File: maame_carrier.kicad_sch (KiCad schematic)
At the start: 18 parts, among them J1 To Kakute H7 V1.5: full left 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, J10 FS-iA10B iBUS servo lead (S +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, J11 TF-Luna pin order 1-6 (CFG ti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, J12 Spare FC I2C (5 V supply, sha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, J13 Payload servo power (+ -); se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, J17 Kakute spare: T3 RSSI 3V3(FC)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, J3 VBAT tap from ESC battery pad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, J4 Micro BEC input leads (6-60 V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, J5 Micro BEC output leads (set t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, J6 Spare power: 5V_AUX G 5V_FC G, J7 Pi expansion: 3V3 logic ONLY, J8 TBS M10Q: order matches its p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, J9 SiK radio (UART4), U1 Raspberry Pi Zero W v1.1, com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

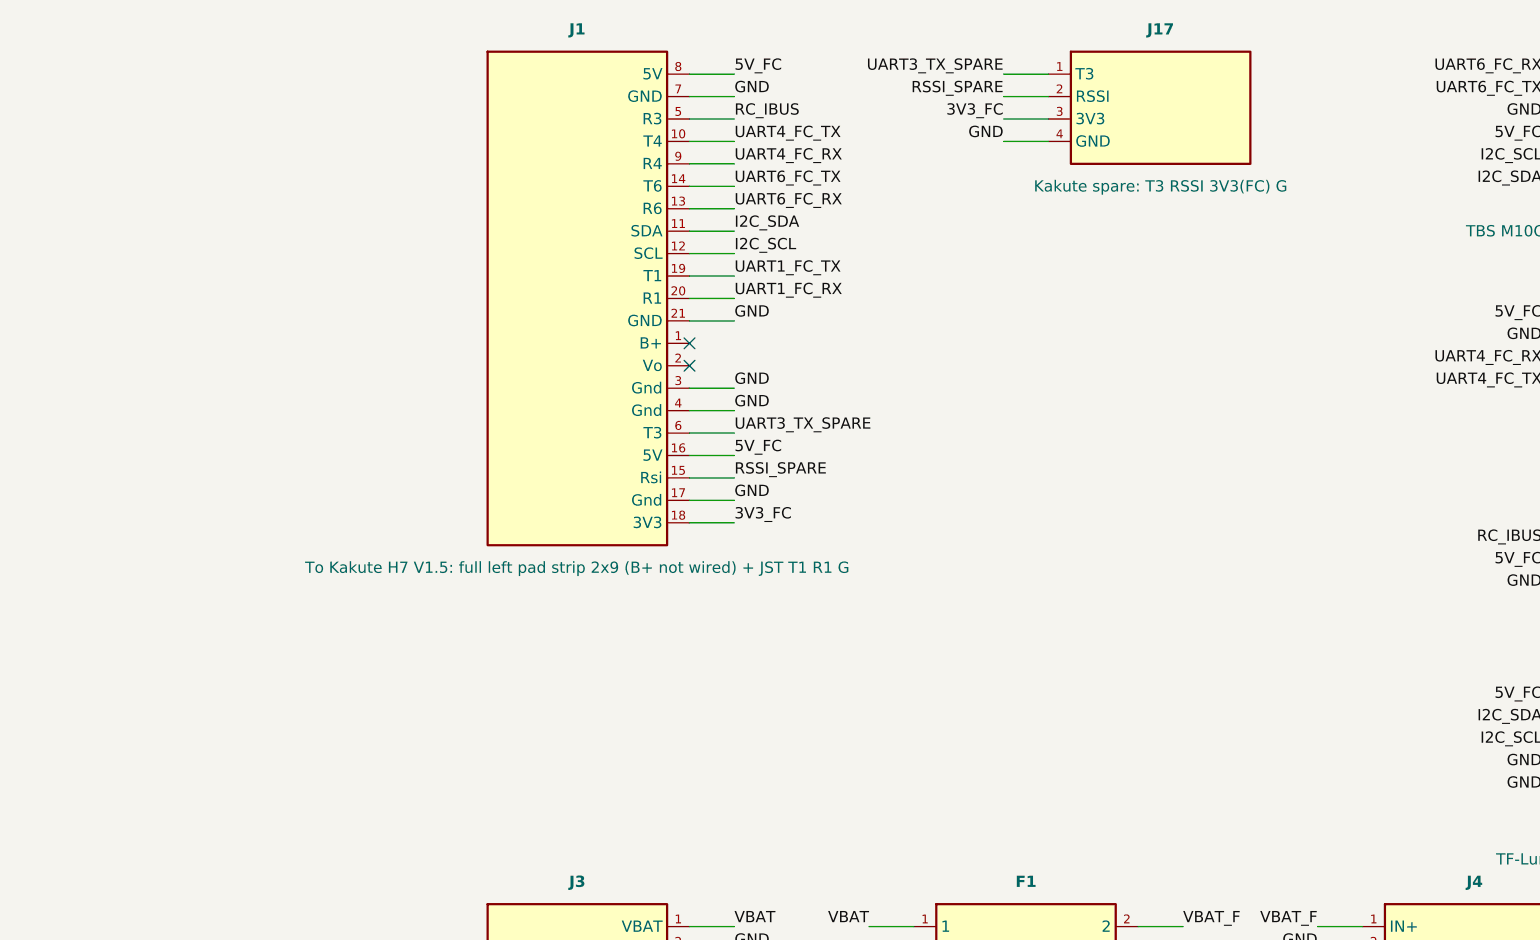
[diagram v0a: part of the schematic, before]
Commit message: J1 mirrors the Kakute's top (G 5V Vi CAM) and bottom (Z- 5V G LED) pad rows; J17 gains BUZ- and LED; J13 under J12; template and render refreshed
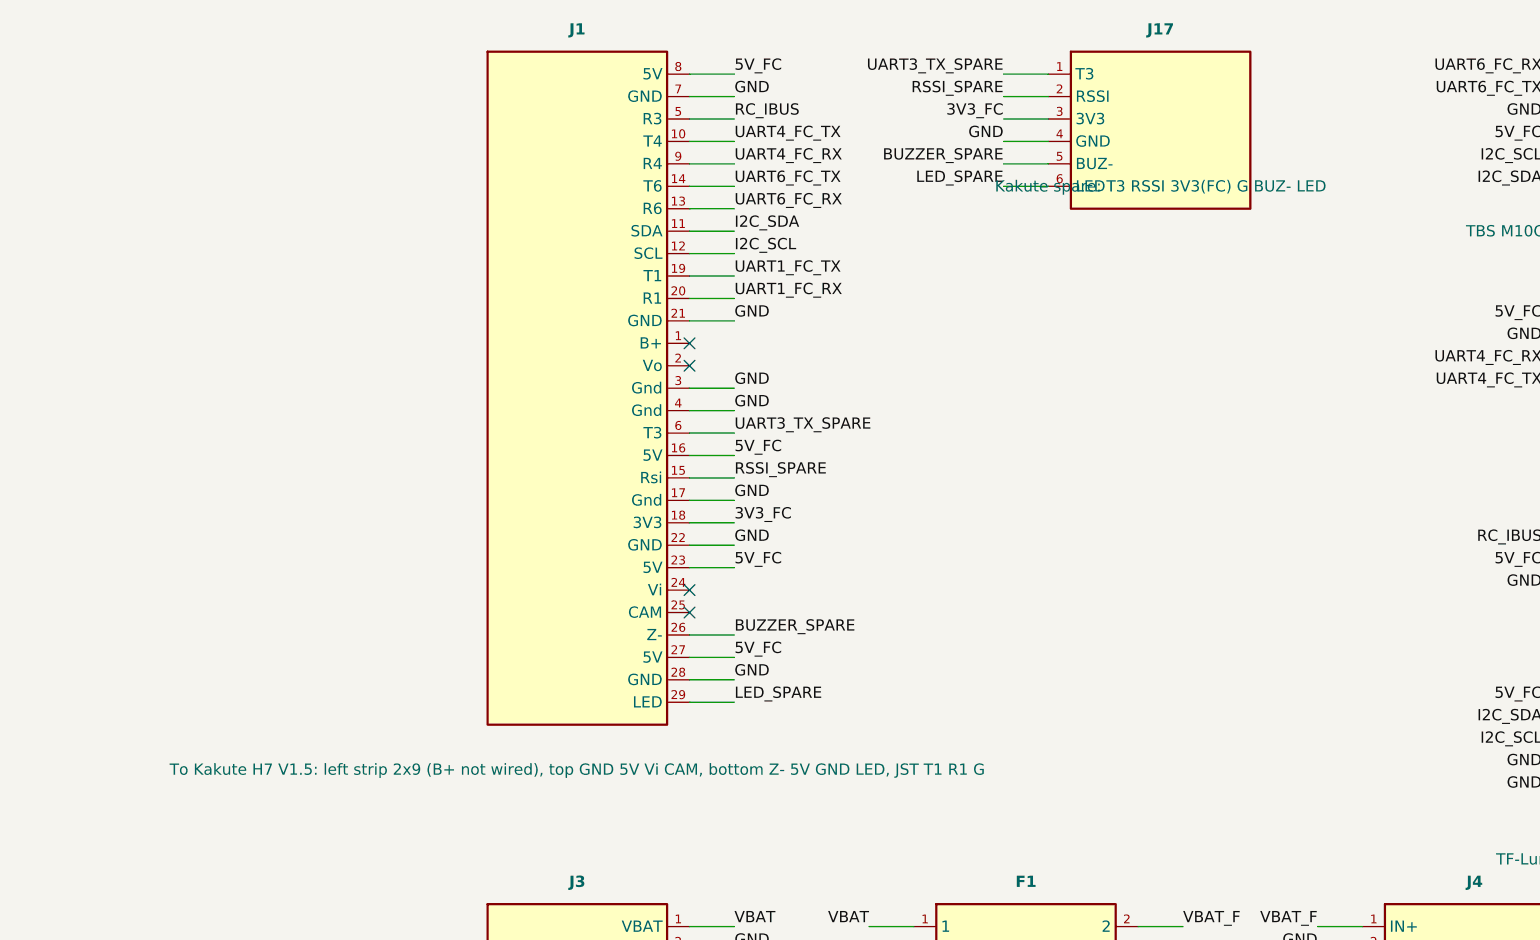
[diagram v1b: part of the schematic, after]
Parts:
- J1: value To Kakute H7 V1.5: full left pad strip 2x9 (B+ not wired) + JST T1 R1 G -> To Kakute H7 V1.5: left strip 2x9 (B+ not wired), top GND 5V Vi CAM, bottom Z- 5V GND LED, JST T1 R1 G
- J17: value Kakute spare: T3 RSSI 3V3(FC) G -> Kakute spare: T3 RSSI 3V3(FC) G BUZ- LED; footprint Connector_PinHeader_2.54mm:PinHeader_1x04_P2.54mm_Vertical -> Connector_PinHeader_2.54mm:PinHeader_1x06_P2.54mm_Vertical
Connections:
- net 5V_FC: now also J1.23 (5V), J1.27 (5V)
- net GND: now also J1.22 (GND), J1.28 (GND)
- new net BUZZER_SPARE: J1.26 (Z-), J17.5 (BUZ-)
- new net LED_SPARE: J1.29 (LED), J17.6 (LED)
- no-connect marks 15 -> 17
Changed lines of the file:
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@@
 			)
 		)
-		(property "Value" "Kakute spare: T3 RSSI 3V3(FC) G"
+		(property "Value" "Kakute spare: T3 RSSI 3V3(FC) G BUZ- LED"
 			(at 116.84 48.26 0)
 			(show_name no)
@@
 			)
 		)
-		(property "Footprint" "Connector_PinHeader_2.54mm:PinHeader_1x04_P2.54mm_Vertical"
+		(property "Footprint" "Connector_PinHeader_2.54mm:PinHeader_1x06_P2.54mm_Vertical"
 			(at 116.84 35.56 0)
 			(hide yes)
@@
 		)
 		(pin "4"
+		)
+		(pin "5"
+		)
+		(pin "6"
 		)
 		(instances
@@
 			)
 		)
-		(property "Value" "To Kakute H7 V1.5: full left pad strip 2x9 (B+ not wired) + JST T1 R1 G"
-			(at 50.8 91.44 0)
+		(property "Value" "To Kakute H7 V1.5: left strip 2x9 (B+ not wired), top GND 5V Vi CAM, bottom Z- 5V GND LED, JST T1 R1 G"
+			(at 50.8 114.3 0)
 			(show_name no)
 			(do_not_autoplace no)
@@
 		)
 		(pin "21"
+		)
+		(pin "22"
+		)
+		(pin "23"
+		)
+		(pin "24"
+		)
+		(pin "25"
+		)
+		(pin "26"
+		)
+		(pin "27"
+		)
+		(pin "28"
+		)
+		(pin "29"
 		)
 		(instances
@@
 		(effects
 			(font
+				(size 1.27 1.27)
+			)
+			(justify right bottom)
+		)
+	)
+	(wire
+		(pts
+			(xy 63.5 88.9) (xy 68.58 88.9)
+		)
+		(stroke
+			(width 0)
+			(type default)
+		)
+	)
+	(label "GND"
+		(at 68.58 88.9 0)
+		(effects
+			(font
+				(size 1.27 1.27)
+			)
+			(justify left bottom)
+		)
+	)
+	(wire
+		(pts
+			(xy 63.5 91.44) (xy 68.58 91.44)
+		)
+		(stroke
+			(width 0)
+			(type default)
+		)
+	)
+	(label "5V_FC"
+		(at 68.58 91.44 0)
+		(effects
+			(font
+				(size 1.27 1.27)
+			)
+			(justify left bottom)
+		)
+	)
+	(no_connect
+		(at 63.5 93.98)
+	)
+	(no_connect
+		(at 63.5 96.52)
+	)
+	(wire
+		(pts
+			(xy 63.5 99.06) (xy 68.58 99.06)
+		)
+		(stroke
+			(width 0)
+			(type default)
+		)
+	)
+	(label "BUZZER_SPARE"
+		(at 68.58 99.06 0)
+		(effects
+			(font
+				(size 1.27 1.27)
+			)
+			(justify left bottom)
+		)
+	)
+	(wire
+		(pts
+			(xy 63.5 101.6) (xy 68.58 101.6)
+		)
+		(stroke
+			(width 0)
+			(type default)
+		)
+	)
+	(label "5V_FC"
+		(at 68.58 101.6 0)
+		(effects
+			(font
+				(size 1.27 1.27)
+			)
+			(justify left bottom)
+		)
+	)
+	(wire
+		(pts
+			(xy 63.5 104.14) (xy 68.58 104.14)
+		)
+		(stroke
+			(width 0)
+			(type default)
+		)
+	)
+	(label "GND"
+		(at 68.58 104.14 0)
+		(effects
+			(font
+				(size 1.27 1.27)
+			)
+			(justify left bottom)
+		)
+	)
+	(wire
+		(pts
+			(xy 63.5 106.68) (xy 68.58 106.68)
+		)
+		(stroke
+			(width 0)
+			(type default)
+		)
+	)
+	(label "LED_SPARE"
+		(at 68.58 106.68 0)
+		(effects
+			(font
+				(size 1.27 1.27)
+			)
+			(justify left bottom)
+		)
+	)
+	(wire
+		(pts
+			(xy 104.14 45.72) (xy 99.06 45.72)
+		)
+		(stroke
+			(width 0)
+			(type default)
+		)
+	)
+	(label "BUZZER_SPARE"
+		(at 99.06 45.72 180)
+		(effects
+			(font
+				(size 1.27 1.27)
+			)
+			(justify right bottom)
+		)
+	)
+	(wire
+		(pts
+			(xy 104.14 48.26) (xy 99.06 48.26)
+		)
+		(stroke
+			(width 0)
+			(type default)
+		)
+	)
+	(label "LED_SPARE"
+		(at 99.06 48.26 180)
+		(effects
+			(font

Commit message: Rounded 3 mm corners; status LED row: FC5V, AUX5V (hardware), PI/DATA/BATT H-M-L on Pi GPIO16/20/19/21/18
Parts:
- added D2: Green 0805: 5V_FC on, LED_SMD:LED_0805_2012Metric_Pad1.15x1.40mm_HandSolder, symbol maame_carrier:LED
- added D3: Green 0805: Pi active (GPIO16), LED_SMD:LED_0805_2012Metric_Pad1.15x1.40mm_HandSolder, symbol maame_carrier:LED
- added D4: Yellow 0805: data (GPIO20), LED_SMD:LED_0805_2012Metric_Pad1.15x1.40mm_HandSolder, symbol maame_carrier:LED
- added D5: Green 0805: battery high (GPIO19), LED_SMD:LED_0805_2012Metric_Pad1.15x1.40mm_HandSolder, symbol maame_carrier:LED
- added D6: Yellow 0805: battery mid (GPIO21), LED_SMD:LED_0805_2012Metric_Pad1.15x1.40mm_HandSolder, symbol maame_carrier:LED
- added D7: Red 0805: battery low (GPIO18), LED_SMD:LED_0805_2012Metric_Pad1.15x1.40mm_HandSolder, symbol maame_carrier:LED
- added R2: 1k 0805, Resistor_SMD:R_0805_2012Metric_Pad1.20x1.40mm_HandSolder, symbol maame_carrier:Resistor
- added R3, R4, R5, R6: 330R 0805, Resistor_SMD:R_0805_2012Metric_Pad1.20x1.40mm_HandSolder, symbol maame_carrier:Resistor
- added R7: 390R 0805, Resistor_SMD:R_0805_2012Metric_Pad1.20x1.40mm_HandSolder, symbol maame_carrier:Resistor
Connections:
- net 5V_FC: now also R2.1
- net GND: now also D2.1 (K), D3.1 (K), D4.1 (K), D5.1 (K), D6.1 (K), D7.1 (K)
- net LED_BATT_LO: now reaches U1.12 (GPIO18)
- net LED_BATT_LO: now also R7.1
- net LED_BATT_HI: now reaches U1.35 (GPIO19)
- net LED_BATT_HI: now also R5.1
- net LED_PI_ACTIVE: now reaches U1.36 (GPIO16)
- net LED_PI_ACTIVE: now also R3.1
- net LED_DATA: now reaches U1.38 (GPIO20)
- net LED_DATA: now also R4.1
- net LED_BATT_MID: now reaches U1.40 (GPIO21)
- net LED_BATT_MID: now also R6.1
- new net LED2_A: D2.2 (A), R2.2
- new net LED3_A: D3.2 (A), R3.2
- new net LED4_A: D4.2 (A), R4.2
- new net LED5_A: D5.2 (A), R5.2
- new net LED6_A: D6.2 (A), R6.2
- new net LED7_A: D7.2 (A), R7.2
- no-connect marks 17 -> 12
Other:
- note added: "9. Status LEDs: D2 FC 5V and D1 AUX 5V are hardware. D3-D7 are driven by Pi software: GPIO16 PI ACTIVE, GPIO20 DATA, GPIO19/21/18 BATT HIGH/MID/LOW (from FC BATTERY_STATUS via MAVLink). They stay off until the Pi script runs."

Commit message: Fab prep: JLC design rules + Power/VBAT net classes; board nets synced to schematic (0 parity issues); THT headers/Pi socket DNP, wire pads out of BOM; frame holes board-only
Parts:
- J1, J10, J11, J12, J13, J17, J6, J7, J8, J9, U1: now not fitted
- J3, J4, J5: now left out of the parts list
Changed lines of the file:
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@@
 		(on_board yes)
 		(in_pos_files yes)
-		(dnp no)
+		(dnp yes)
 		(property "Reference" "J12"
 			(at 241.3 30.48 0)
@@
 		(on_board yes)
 		(in_pos_files yes)
-		(dnp no)
+		(dnp yes)
 		(property "Reference" "J17"
 			(at 116.84 30.48 0)
@@
 		(on_board yes)
 		(in_pos_files yes)
-		(dnp no)
+		(dnp yes)
 		(property "Reference" "J9"
 			(at 177.8 58.42 0)
@@
 		(on_board yes)
 		(in_pos_files yes)
-		(dnp no)
+		(dnp yes)
 		(property "Reference" "U1"
 			(at 330.2 30.48 0)
@@
 		(on_board yes)
 		(in_pos_files yes)
-		(dnp no)
+		(dnp yes)
 		(property "Reference" "J1"
 			(at 50.8 30.48 0)
@@
 		(on_board yes)
 		(in_pos_files yes)
-		(dnp no)
+		(dnp yes)
 		(property "Reference" "J11"
 			(at 177.8 101.6 0)
@@
 		(on_board yes)
 		(in_pos_files yes)
-		(dnp no)
+		(dnp yes)
 		(property "Reference" "J6"
 			(at 101.6 157.48 0)
@@
 		(on_board yes)
 		(in_pos_files yes)
-		(dnp no)
+		(dnp yes)
 		(property "Reference" "J10"
 			(at 177.8 83.82 0)
@@
 		(on_board yes)
 		(in_pos_files yes)
-		(dnp no)
+		(dnp yes)
 		(property "Reference" "J7"
 			(at 355.6 157.48 0)
@@
 		(body_style 1)
 		(exclude_from_sim no)
-		(in_bom yes)
+		(in_bom no)
 		(on_board yes)
 		(in_pos_files yes)
@@
 		(on_board yes)
 		(in_pos_files yes)
-		(dnp no)
+		(dnp yes)
 		(property "Reference" "J8"
 			(at 177.8 30.48 0)
@@
 		(on_board yes)
 		(in_pos_files yes)
-		(dnp no)
+		(dnp yes)
 		(property "Reference" "J13"
 			(at 241.3 50.8 0)
@@
 		(body_style 1)
 		(exclude_from_sim no)
-		(in_bom yes)
+		(in_bom no)
 		(on_board yes)
 		(in_pos_files yes)
@@
 		(body_style 1)
 		(exclude_from_sim no)
-		(in_bom yes)
-		(on_board yes)
-		(in_pos_files yes)
+		(in_bom no)
+		(on_board yes)
+		(in_pos_files yes)

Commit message: C1 -> SMD 470uF 16V 6.3x7.7 (LCSC C22383803); LCSC fields on all assembled parts
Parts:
- C1: value 470uF 10V low-ESR (servo/Pi rail) -> 470uF 16V SMD electrolytic (LCSC C22383803); footprint Capacitor_THT:CP_Radial_D8.0mm_P3.50mm -> Capacitor_SMD:CP_Elec_6.3x7.7; LCSC (none) -> C22383803
- D1, D2, D3, D5: LCSC (none) -> C2297
- D4, D6: LCSC (none) -> C2296
- D7: LCSC (none) -> C84256
- F1: LCSC (none) -> C70119
- R1, R2: LCSC (none) -> C17513
- R3, R4, R5, R6: LCSC (none) -> C17630
- R7: LCSC (none) -> C17655
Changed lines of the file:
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@@
 			)
 		)
+		(property "LCSC" "C2297"
+			(at 254 147.32 0)
+			(hide yes)
+			(show_name no)
+			(do_not_autoplace no)
+			(effects
+				(font
+					(size 1.27 1.27)
+				)
+			)
+		)
 		(pin "2"
 		)
@@
 			)
 		)
-		(property "Value" "470uF 10V low-ESR (servo/Pi rail)"
+		(property "Value" "470uF 16V SMD electrolytic (LCSC C22383803)"
 			(at 203.2 137.16 0)
 			(show_name no)
@@
 			)
 		)
-		(property "Footprint" "Capacitor_THT:CP_Radial_D8.0mm_P3.50mm"
+		(property "Footprint" "Capacitor_SMD:CP_Elec_6.3x7.7"
 			(at 203.2 132.08 0)
 			(hide yes)
@@
 			)
 		)
+		(property "LCSC" "C22383803"
+			(at 203.2 132.08 0)
+			(hide yes)
+			(show_name no)
+			(do_not_autoplace no)
+			(effects
+				(font
+					(size 1.27 1.27)
+				)
+			)
+		)
 		(pin "1"
 		)
@@
 			)
 		)
+		(property "LCSC" "C70119"
+			(at 101.6 132.08 0)
+			(hide yes)
+			(show_name no)
+			(do_not_autoplace no)
+			(effects
+				(font
+					(size 1.27 1.27)
+				)
+			)
+		)
 		(pin "1"
 		)
@@
 			)
 		)
+		(property "LCSC" "C17513"
+			(at 203.2 147.32 0)
+			(hide yes)
+			(show_name no)
+			(do_not_autoplace no)
+			(effects
+				(font
+					(size 1.27 1.27)
+				)
+			)
+		)
 		(pin "1"
 		)
@@
 			)
 		)
+		(property "LCSC" "C17513"
+			(at 203.2 154.94 0)
+			(hide yes)
+			(show_name no)
+			(do_not_autoplace no)
+			(effects
+				(font
+					(size 1.27 1.27)
+				)
+			)
+		)
 		(pin "1"
 		)
@@
 			)
 		)
+		(property "LCSC" "C2297"
+			(at 254 154.94 0)
+			(hide yes)
+			(show_name no)
+			(do_not_autoplace no)
+			(effects
+				(font
+					(size 1.27 1.27)
+				)
+			)
+		)
 		(pin "2"
 		)
@@
 			)
 		)
+		(property "LCSC" "C17630"
+			(at 203.2 162.56 0)
+			(hide yes)
+			(show_name no)
+			(do_not_autoplace no)
+			(effects
+				(font
+					(size 1.27 1.27)
+				)
+			)
+		)
 		(pin "1"
 		)
@@
 			)
 		)
+		(property "LCSC" "C2297"
+			(at 254 162.56 0)
+			(hide yes)
+			(show_name no)
+			(do_not_autoplace no)
+			(effects
+				(font
+					(size 1.27 1.27)
+				)
+			)
+		)
 		(pin "2"
 		)
@@
 			)
 		)
+		(property "LCSC" "C17630"
+			(at 203.2 170.18 0)
+			(hide yes)
+			(show_name no)
+			(do_not_autoplace no)
+			(effects
+				(font
+					(size 1.27 1.27)
+				)
+			)
+		)
 		(pin "1"
 		)
@@
 			)
 		)
+		(property "LCSC" "C2296"
+			(at 254 170.18 0)
+			(hide yes)
+			(show_name no)
+			(do_not_autoplace no)
+			(effects
+				(font
+					(size 1.27 1.27)
+				)
+			)
+		)
 		(pin "2"
 		)
@@
 			)
 		)
+		(property "LCSC" "C17630"
+			(at 203.2 177.8 0)
+			(hide yes)
+			(show_name no)
+			(do_not_autoplace no)
+			(effects
+				(font
+					(size 1.27 1.27)
+				)
+			)
+		)
 		(pin "1"
 		)
@@
 			)
 		)
+		(property "LCSC" "C2297"
+			(at 254 177.8 0)
+			(hide yes)
+			(show_name no)
+			(do_not_autoplace no)
+			(effects
+				(font
+					(size 1.27 1.27)
+				)
+			)
+		)
 		(pin "2"
 		)
@@
 			)
 		)
+		(property "LCSC" "C17630"
+			(at 203.2 185.42 0)
+			(hide yes)
+			(show_name no)
+			(do_not_autoplace no)
+			(effects
+				(font
+					(size 1.27 1.27)
+				)
+			)
+		)
 		(pin "1"
 		)
@@
 			)
 		)
+		(property "LCSC" "C2296"
+			(at 254 185.42 0)
+			(hide yes)
+			(show_name no)
+			(do_not_autoplace no)
+			(effects
+				(font
+					(size 1.27 1.27)
+				)
+			)
+		)
 		(pin "2"
 		)
@@
 			)
 		)
+		(property "LCSC" "C17655"
+			(at 203.2 193.04 0)
+			(hide yes)
+			(show_name no)
+			(do_not_autoplace no)
+			(effects
+				(font
+					(size 1.27 1.27)
+				)
+			)
+		)
 		(pin "1"
 		)
@@
 			(show_name no)
 			(do_not_autoplace no)
+			(effects
+				(font
+					(size 1.27 1.27)
+				)
+			)
+		)
+		(property "LCSC" "C84256"
+			(at 254 193.04 0)
+			(hide yes)
+			(show_name no)
+			(do_not_autoplace no)

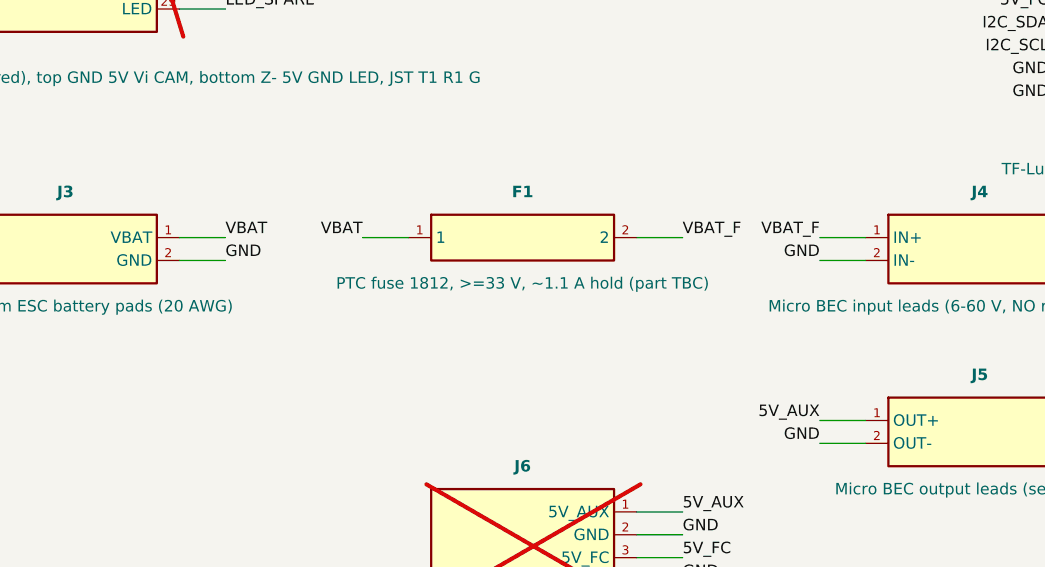
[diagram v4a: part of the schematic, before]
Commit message: JLCPCB package in fab/: Gerbers + Excellon (zip), BOM and CPL CSVs, top/bottom renders; F1 set to TECHFUSE mSMD110-33V (C70119)
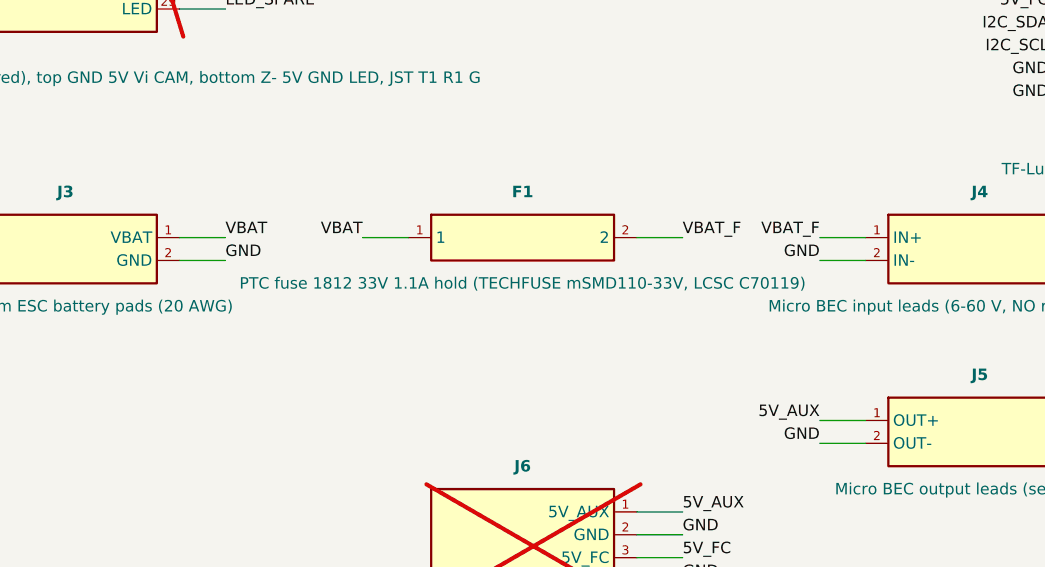
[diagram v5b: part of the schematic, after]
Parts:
- F1: value PTC fuse 1812, >=33 V, ~1.1 A hold (part TBC) -> PTC fuse 1812 33V 1.1A hold (TECHFUSE mSMD110-33V, LCSC C70119)
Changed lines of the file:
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@@
 			)
 		)
-		(property "Value" "PTC fuse 1812, >=33 V, ~1.1 A hold (part TBC)"
+		(property "Value" "PTC fuse 1812 33V 1.1A hold (TECHFUSE mSMD110-33V, LCSC C70119)"
 			(at 101.6 137.16 0)
 			(show_name no)
